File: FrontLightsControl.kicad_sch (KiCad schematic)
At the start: 0 parts

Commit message: Integration of changes into prewious style of schematic
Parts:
- added C47, C48, C49, C50: 100nF, PCM_JLCPCB:C_0805, symbol PCM_JLCPCB-Capacitors:0805,100nF,(2)
- added D3: BAT54S_C7420333, PCM_JLCPCB:SOT-23-3_L2.9-W1.3-P1.90-LS2.4-BR, symbol PCM_JLCPCB-Diode-Packages:Schottky, BAT54S_C7420333
- added D4: 1N4148W, PCM_JLCPCB:D_SOD-123, symbol PCM_JLCPCB-Diodes:Switching,1N4148W
- added J5: Conn_01x09, symbol Connector_Generic:Conn_01x09
- added R26, R27, R28, R29, R30, R31: 1kΩ, PCM_JLCPCB:R_0805, symbol PCM_JLCPCB-Resistors:0805,1kΩ
- added R32: 4.7kΩ, PCM_JLCPCB:R_0805, symbol PCM_JLCPCB-Resistors:0805,4.7kΩ
- added U3, U5, U6, U7: VND7050AJTR, easyeda2kicad:POWERSSO-16_L4.9-W3.9-P0.50-LS6.0-BL-EP, symbol easyeda2kicad:VND7050AJTR
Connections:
- new net: J5.5 (Pin_5), U5.10 (OUTPUT1), U5.11 (OUTPUT1), U5.12 (OUTPUT1), U5.9 (OUTPUT1)
- new net: J5.4 (Pin_4), U5.13 (OUTPUT0), U5.14 (OUTPUT0), U5.15 (OUTPUT0), U5.16 (OUTPUT0)
- new net: R27.2, U3.2 (~{FaultRST}), U5.2 (~{FaultRST}), U6.2 (~{FaultRST}), U7.2 (~{FaultRST})
- new net: D4.2, R32.1, U3.4 (GND), U5.4 (GND), U6.4 (GND), U7.4 (GND)
- new net: R28.2, U3.5 (SEL0), U5.5 (SEL0), U6.5 (SEL0), U7.5 (SEL0)
- new net: R29.2, U3.6 (SEL1), U5.6 (SEL1), U6.6 (SEL1), U7.6 (SEL1)
- new net: R30.2, R31.1, U3.7 (MultiSense), U5.7 (MultiSense), U6.7 (MultiSense), U7.7 (MultiSense)
- new net: J5.9 (Pin_9), U7.10 (OUTPUT1), U7.11 (OUTPUT1), U7.12 (OUTPUT1), U7.9 (OUTPUT1)
- new net: J5.8 (Pin_8), U7.13 (OUTPUT0), U7.14 (OUTPUT0), U7.15 (OUTPUT0), U7.16 (OUTPUT0)
- new net: J5.3 (Pin_3), U3.10 (OUTPUT1), U3.11 (OUTPUT1), U3.12 (OUTPUT1), U3.9 (OUTPUT1)
- new net: J5.2 (Pin_2), U3.13 (OUTPUT0), U3.14 (OUTPUT0), U3.15 (OUTPUT0), U3.16 (OUTPUT0)
- new net: J5.6 (Pin_6), U6.13 (OUTPUT0), U6.14 (OUTPUT0), U6.15 (OUTPUT0), U6.16 (OUTPUT0)
- new net: J5.7 (Pin_7), U6.10 (OUTPUT1), U6.11 (OUTPUT1), U6.12 (OUTPUT1), U6.9 (OUTPUT1)
- new net +12V: C47.1, C48.1, C49.1, C50.1, U3.17 (VCC), U5.17 (VCC), U6.17 (VCC), U7.17 (VCC)
- new net +3.3V: D3.2 (K2), R26.2
- new net GND: C47.2, C48.2, C49.2, C50.2, D3.1 (K1), D4.1, J5.1 (Pin_1), R31.2, R32.2
- new net SEL0: R28.1
- new net SEL1: R29.1
- new net Sense: D3.3 (A), R30.1
- new net output0: U3.1 (INPUT0)
- new net output1: U3.8 (INPUT1)
- new net output2: U5.1 (INPUT0)
- new net output3: U5.8 (INPUT1)
- new net output4: U6.1 (INPUT0)
- new net output5: U6.8 (INPUT1)
- new net output6: U7.1 (INPUT0)
- new net output7: U7.8 (INPUT1)
- new net selA: U3.3 (SEn)
- new net selB: U5.3 (SEn)
- new net selC: U6.3 (SEn)
- new net selD: U7.3 (SEn)
- new net ~{FaultRST}: R26.1, R27.1
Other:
- note added: "12*12mA = 144mA peak Diode = 150mA nominal"
- note added: "Ground Front position lamp Front direction-indicator lamp, right Front direction-indicator lamp, left Passing-beam headlamp Driving-beam headlamp Daytime running lamp Audible warning device NA"
- note added: "Per datasheet"
- note added: "front connector"

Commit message: I/O Schematic rebuild from DRAFT by Nathann
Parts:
- U3, U5, U6, U7: footprint easyeda2kicad:POWERSSO-16_L4.9-W3.9-P0.50-LS6.0-BL-EP -> Package_SO:PowerSSO-16-1EP_3.9x4.9mm_P0.5mm_EP2.5x3.61mm
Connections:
- net PassingBeamLampOUT: now reaches J5.5 (Pin_5), U5.10 (OUTPUT1), U5.11 (OUTPUT1), U5.12 (OUTPUT1), U5.9 (OUTPUT1)
- net FrontDirLampLeftOUT: now reaches J5.4 (Pin_4), U5.13 (OUTPUT0), U5.14 (OUTPUT0), U5.15 (OUTPUT0), U5.16 (OUTPUT0)
- net Reserved3OUT: now reaches J5.9 (Pin_9), U7.10 (OUTPUT1), U7.11 (OUTPUT1), U7.12 (OUTPUT1), U7.9 (OUTPUT1)
- net AudibleWarnOUT: now reaches J5.8 (Pin_8), U7.13 (OUTPUT0), U7.14 (OUTPUT0), U7.15 (OUTPUT0), U7.16 (OUTPUT0)
- net FrontDirLampRightOUT: now reaches J5.3 (Pin_3), U3.10 (OUTPUT1), U3.11 (OUTPUT1), U3.12 (OUTPUT1), U3.9 (OUTPUT1)
- net FrontPosLampOUT: now reaches J5.2 (Pin_2), U3.13 (OUTPUT0), U3.14 (OUTPUT0), U3.15 (OUTPUT0), U3.16 (OUTPUT0)
- net DrivingBeamLampOUT: now reaches J5.6 (Pin_6), U6.13 (OUTPUT0), U6.14 (OUTPUT0), U6.15 (OUTPUT0), U6.16 (OUTPUT0)
- net DaytimeLampOUT: now reaches J5.7 (Pin_7), U6.10 (OUTPUT1), U6.11 (OUTPUT1), U6.12 (OUTPUT1), U6.9 (OUTPUT1)
- net SEL0 renamed FrontOutSEL0
- net SEL1 renamed FrontOutSEL1
- net Sense renamed FrontSense
- net output0 renamed FrontPosLamp
- net output1 renamed FrontDirLampR
- net output2 renamed FrontDirLampL
- net output3 renamed PassingBeamLamp
- net output4 renamed DrivingBeamLamp
- net output5 renamed DaytimeLamp
- net output6 renamed AudibleWarn
- net output7 renamed Reserved3
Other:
- moved on the sheet: C47, C48, C49, C50, J5

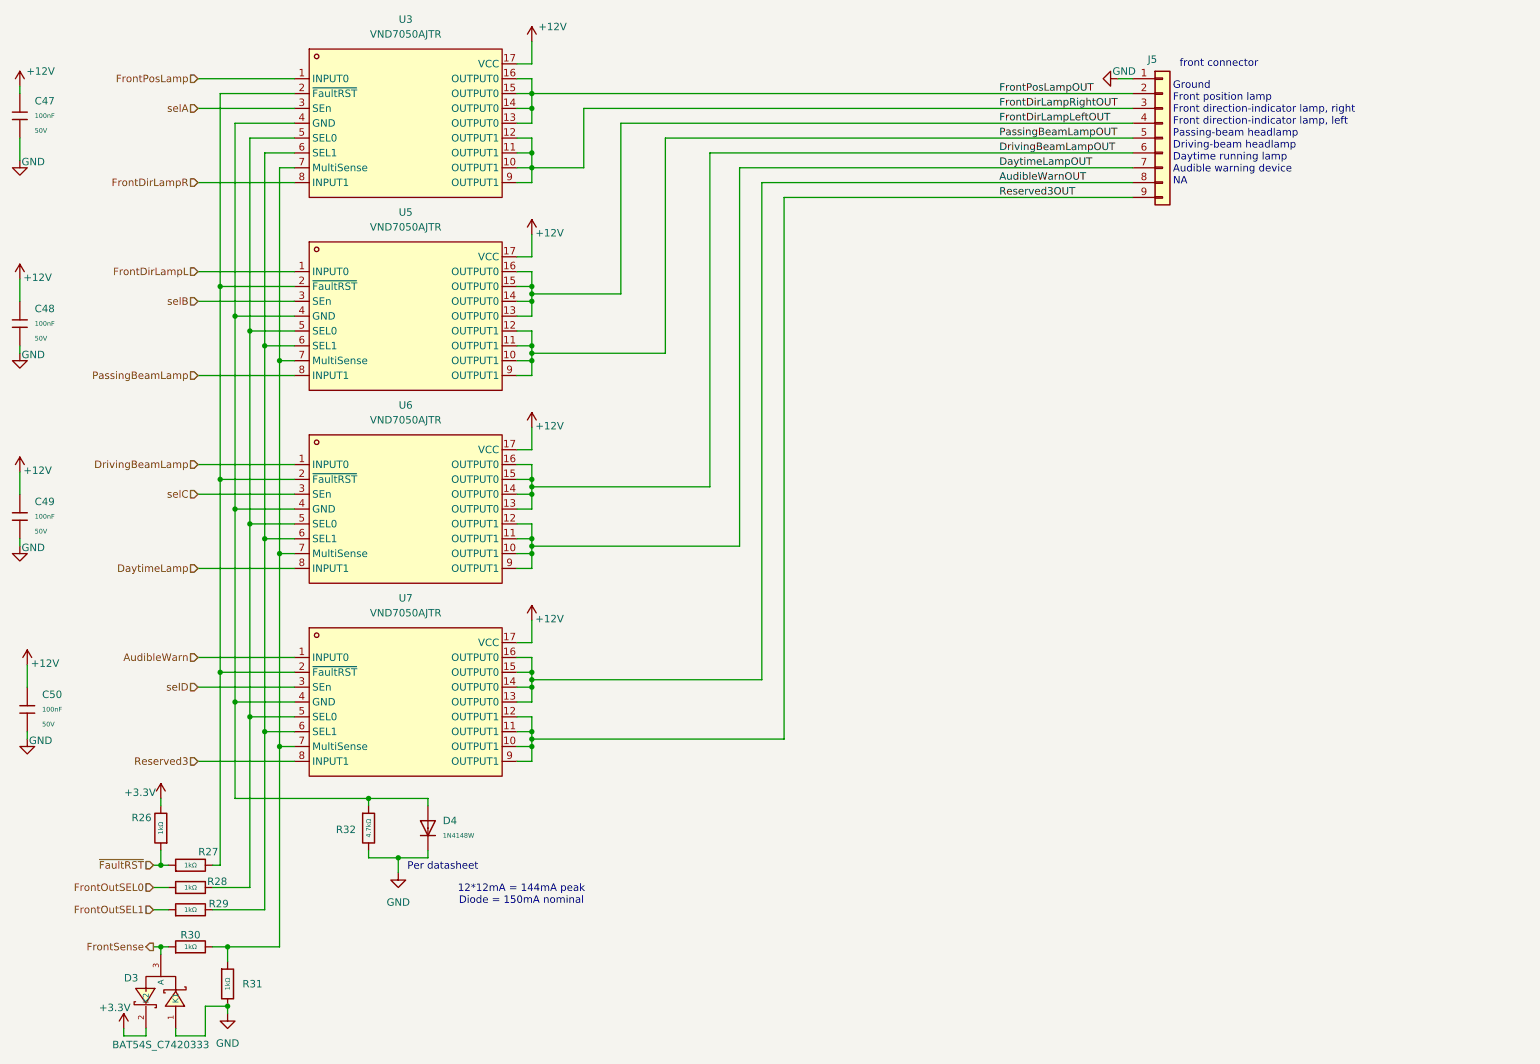
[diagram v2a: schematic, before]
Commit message: EMI/EMC meassures implementation + VCU panel interface block
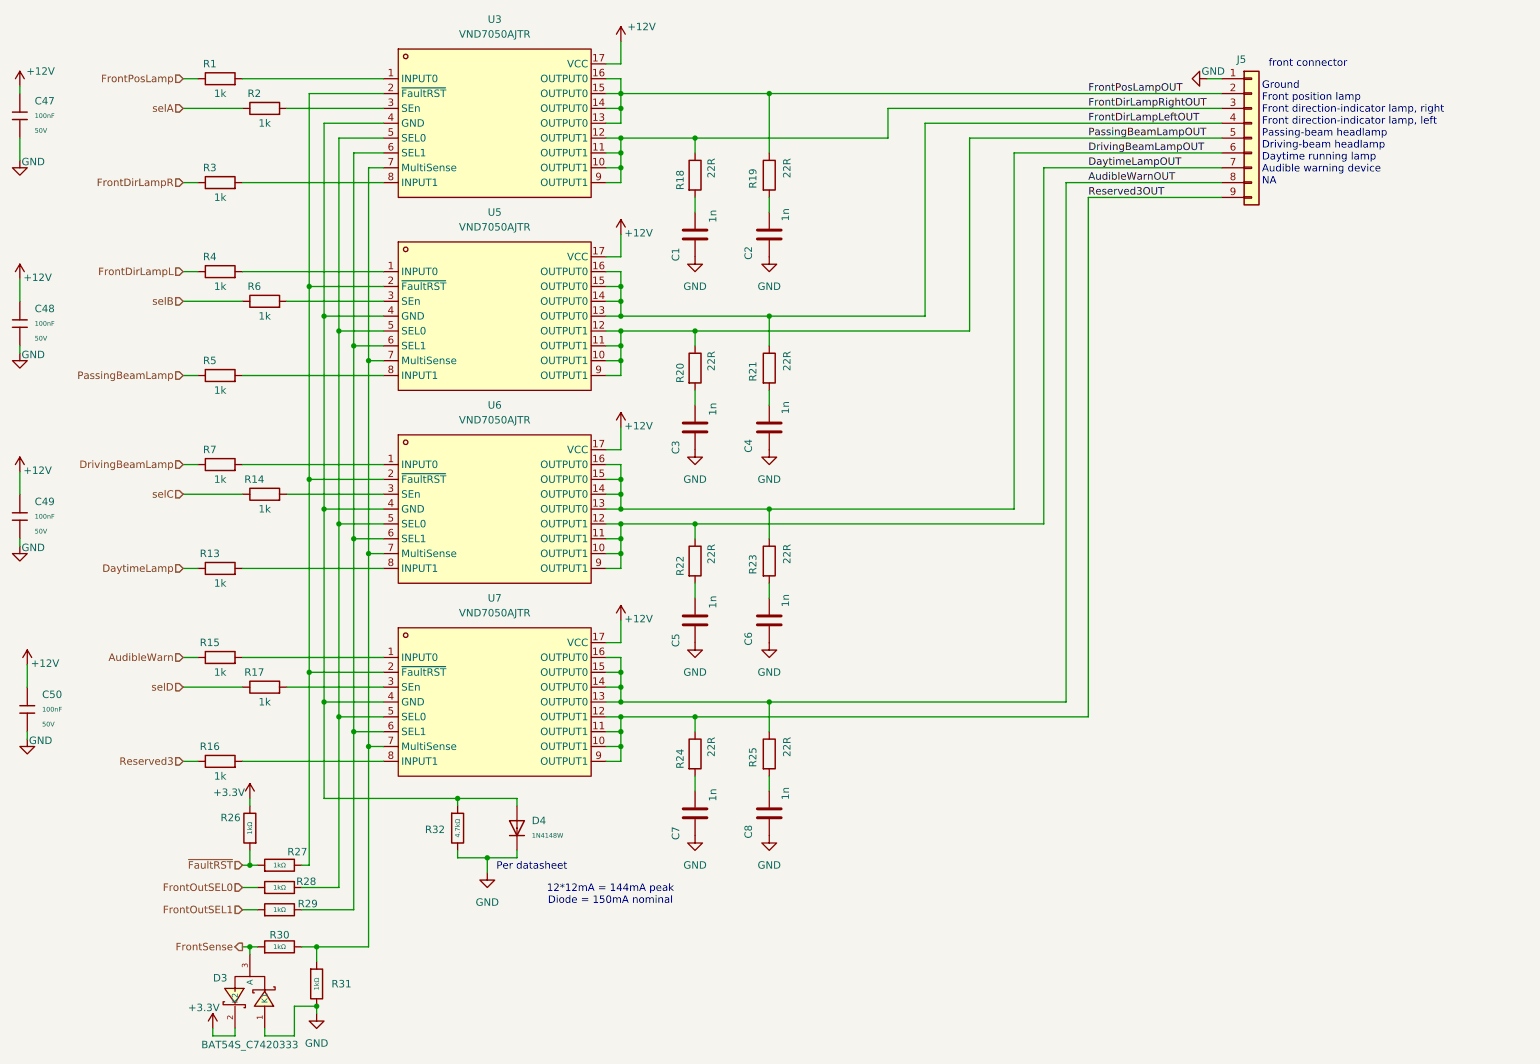
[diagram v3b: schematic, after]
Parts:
- added C1, C2, C3, C4, C5, C6, C7, C8: 1n, Capacitor_SMD:C_0603_1608Metric, symbol VELION_VCU_Library:C
- added R1, R13, R14, R15, R16, R17, R2, R3, R4, R5, R6, R7: 1k, Resistor_SMD:R_0603_1608Metric, symbol VELION_VCU_Library:R
- added R18, R19, R20, R21, R22, R23, R24, R25: 22R, Resistor_SMD:R_0603_1608Metric, symbol VELION_VCU_Library:R
- C47, C48, C49, C50: footprint PCM_JLCPCB:C_0805 -> Capacitor_SMD:C_0603_1608Metric; symbol PCM_JLCPCB-Capacitors:0805,100nF,(2) -> VELION_VCU_Library:0805,100nF,(2)
- D3: footprint PCM_JLCPCB:SOT-23-3_L2.9-W1.3-P1.90-LS2.4-BR -> Package_TO_SOT_SMD:SOT-23-3; symbol PCM_JLCPCB-Diode-Packages:Schottky, BAT54S_C7420333 -> VELION_VCU_Library:Schottky, BAT54S_C7420333
- D4: footprint PCM_JLCPCB:D_SOD-123 -> Diode_SMD:D_SOD-123; symbol PCM_JLCPCB-Diodes:Switching,1N4148W -> VELION_VCU_Library:Switching,1N4148W
- J5: footprint (none) -> Package_TO_SOT_SMD:SOT-23-3; symbol Connector_Generic:Conn_01x09 -> VELION_VCU_Library:Conn_01x09
- R26, R27, R28, R29, R30, R31: footprint PCM_JLCPCB:R_0805 -> Resistor_SMD:R_0805_2012Metric; symbol PCM_JLCPCB-Resistors:0805,1kΩ -> VELION_VCU_Library:0805,1kΩ
- R32: footprint PCM_JLCPCB:R_0805 -> Resistor_SMD:R_0805_2012Metric; symbol PCM_JLCPCB-Resistors:0805,4.7kΩ -> VELION_VCU_Library:0805,4.7kΩ
- U3, U5, U6, U7: symbol easyeda2kicad:VND7050AJTR -> VELION_VCU_Library:VND7050AJTR
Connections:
- net AudibleWarn: now also R15.1; no longer U7.1 (INPUT0)
- net AudibleWarnOUT: now also R25.1
- net DaytimeLamp: now also R13.1; no longer U6.8 (INPUT1)
- net DaytimeLampOUT: now also R22.1
- net DrivingBeamLamp: now also R7.1; no longer U6.1 (INPUT0)
- net DrivingBeamLampOUT: now also R23.1
- net FrontDirLampL: now also R4.1; no longer U5.1 (INPUT0)
- net FrontDirLampLeftOUT: now also R21.1
- net FrontDirLampR: now also R3.1; no longer U3.8 (INPUT1)
- net FrontDirLampRightOUT: now also R18.1
- net FrontPosLamp: now also R1.1; no longer U3.1 (INPUT0)
- net FrontPosLampOUT: now also R19.1
- net GND: now also C1.2, C2.2, C3.2, C4.2, C5.2, C6.2, C7.2, C8.2
- net PassingBeamLamp: now also R5.1; no longer U5.8 (INPUT1)
- net PassingBeamLampOUT: now also R20.1
- net Reserved3: now also R16.1; no longer U7.8 (INPUT1)
- net Reserved3OUT: now also R24.1
- net selA: now also R2.1; no longer U3.3 (SEn)
- net selB: now also R6.1; no longer U5.3 (SEn)
- net selC: now also R14.1; no longer U6.3 (SEn)
- net selD: now also R17.1; no longer U7.3 (SEn)
- new net: C6.1, R23.2
- new net: C4.1, R21.2
- new net: R4.2, U5.1 (INPUT0)
- new net: R6.2, U5.3 (SEn)
- new net: R5.2, U5.8 (INPUT1)
- new net: C5.1, R22.2
- new net: R7.2, U6.1 (INPUT0)
- new net: R3.2, U3.8 (INPUT1)
- new net: C1.1, R18.2
- new net: R15.2, U7.1 (INPUT0)
- new net: R17.2, U7.3 (SEn)
- new net: R16.2, U7.8 (INPUT1)
- new net: C8.1, R25.2
- new net: C2.1, R19.2
- new net: R2.2, U3.3 (SEn)
- new net: R1.2, U3.1 (INPUT0)
- new net: R14.2, U6.3 (SEn)
- new net: C3.1, R20.2
- new net: R13.2, U6.8 (INPUT1)
- new net: C7.1, R24.2
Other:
- moved on the sheet: D3, D4, J5, R26, R27, R28, R29, R30, R31, R32, U3, U5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
